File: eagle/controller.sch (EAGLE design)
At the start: 4 parts, among them IC1 MAX7219CNG

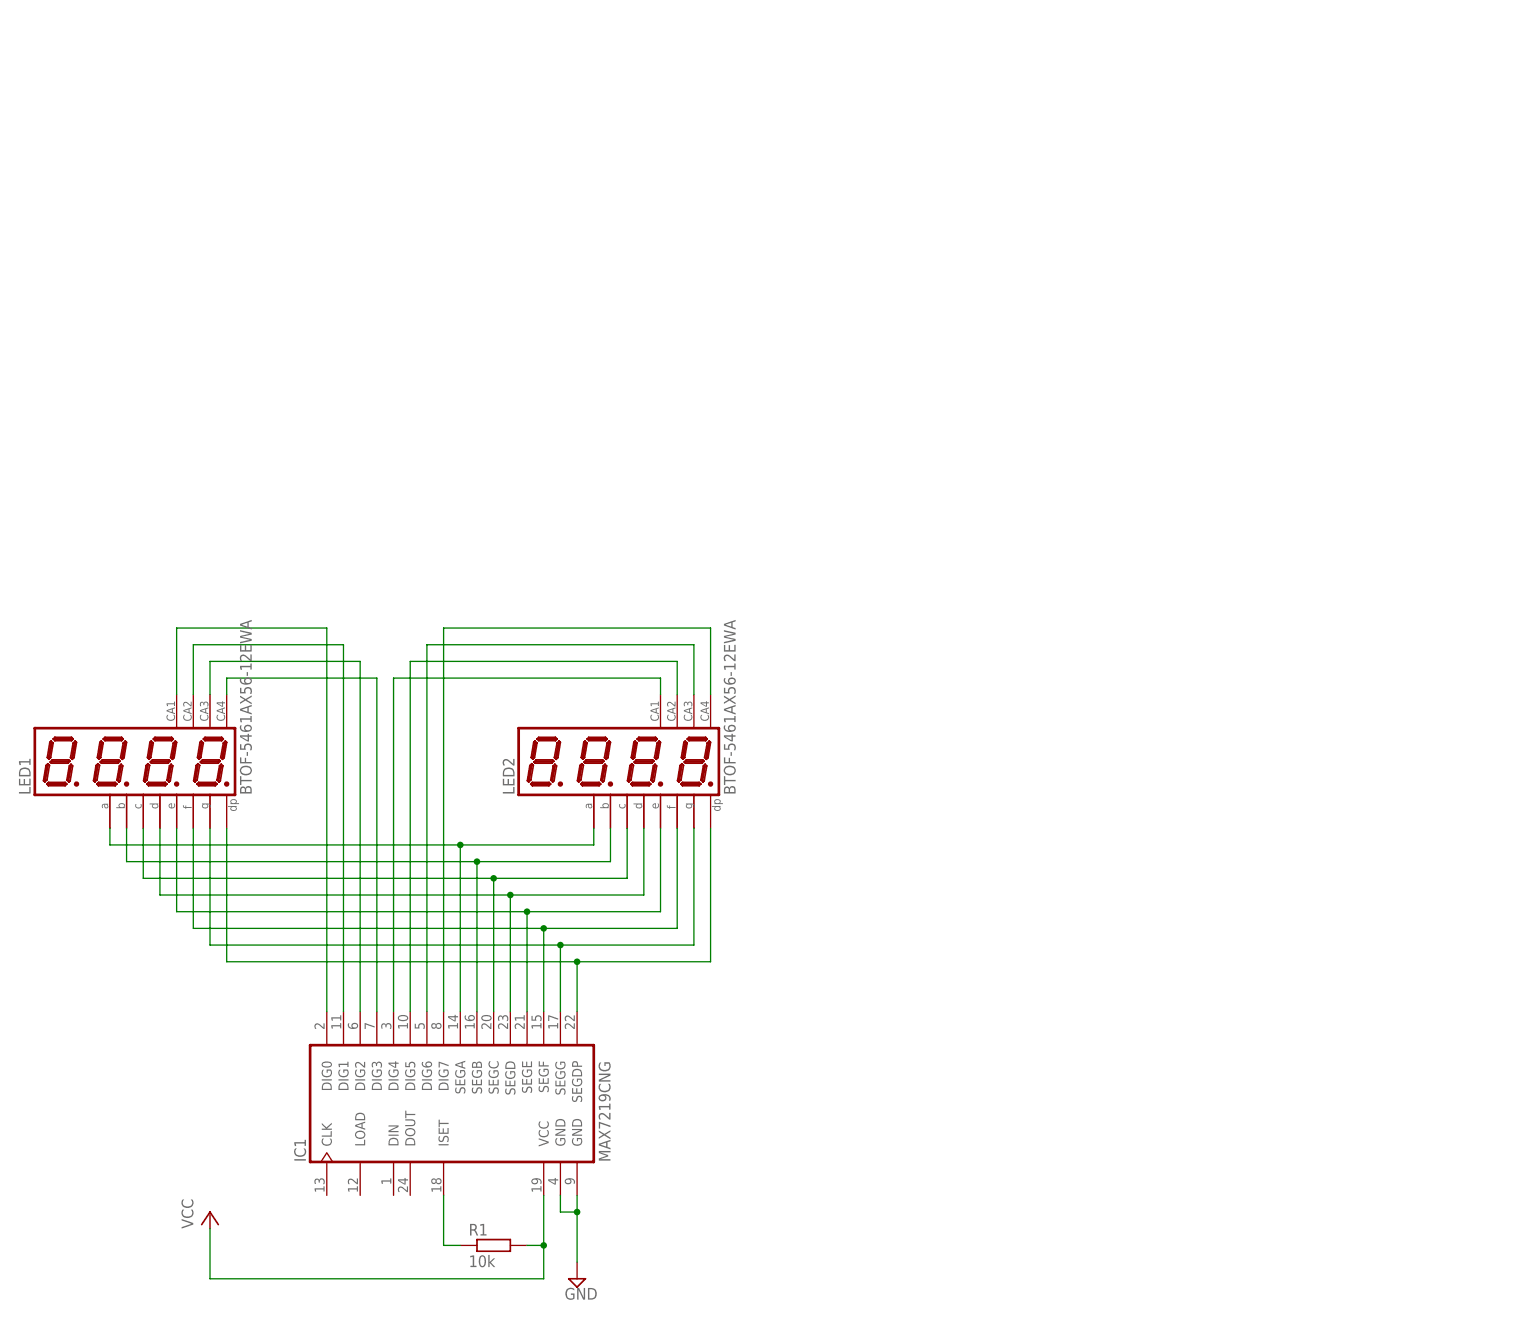
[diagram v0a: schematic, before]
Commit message: Add microcontroller to controller board schematic (still wip)
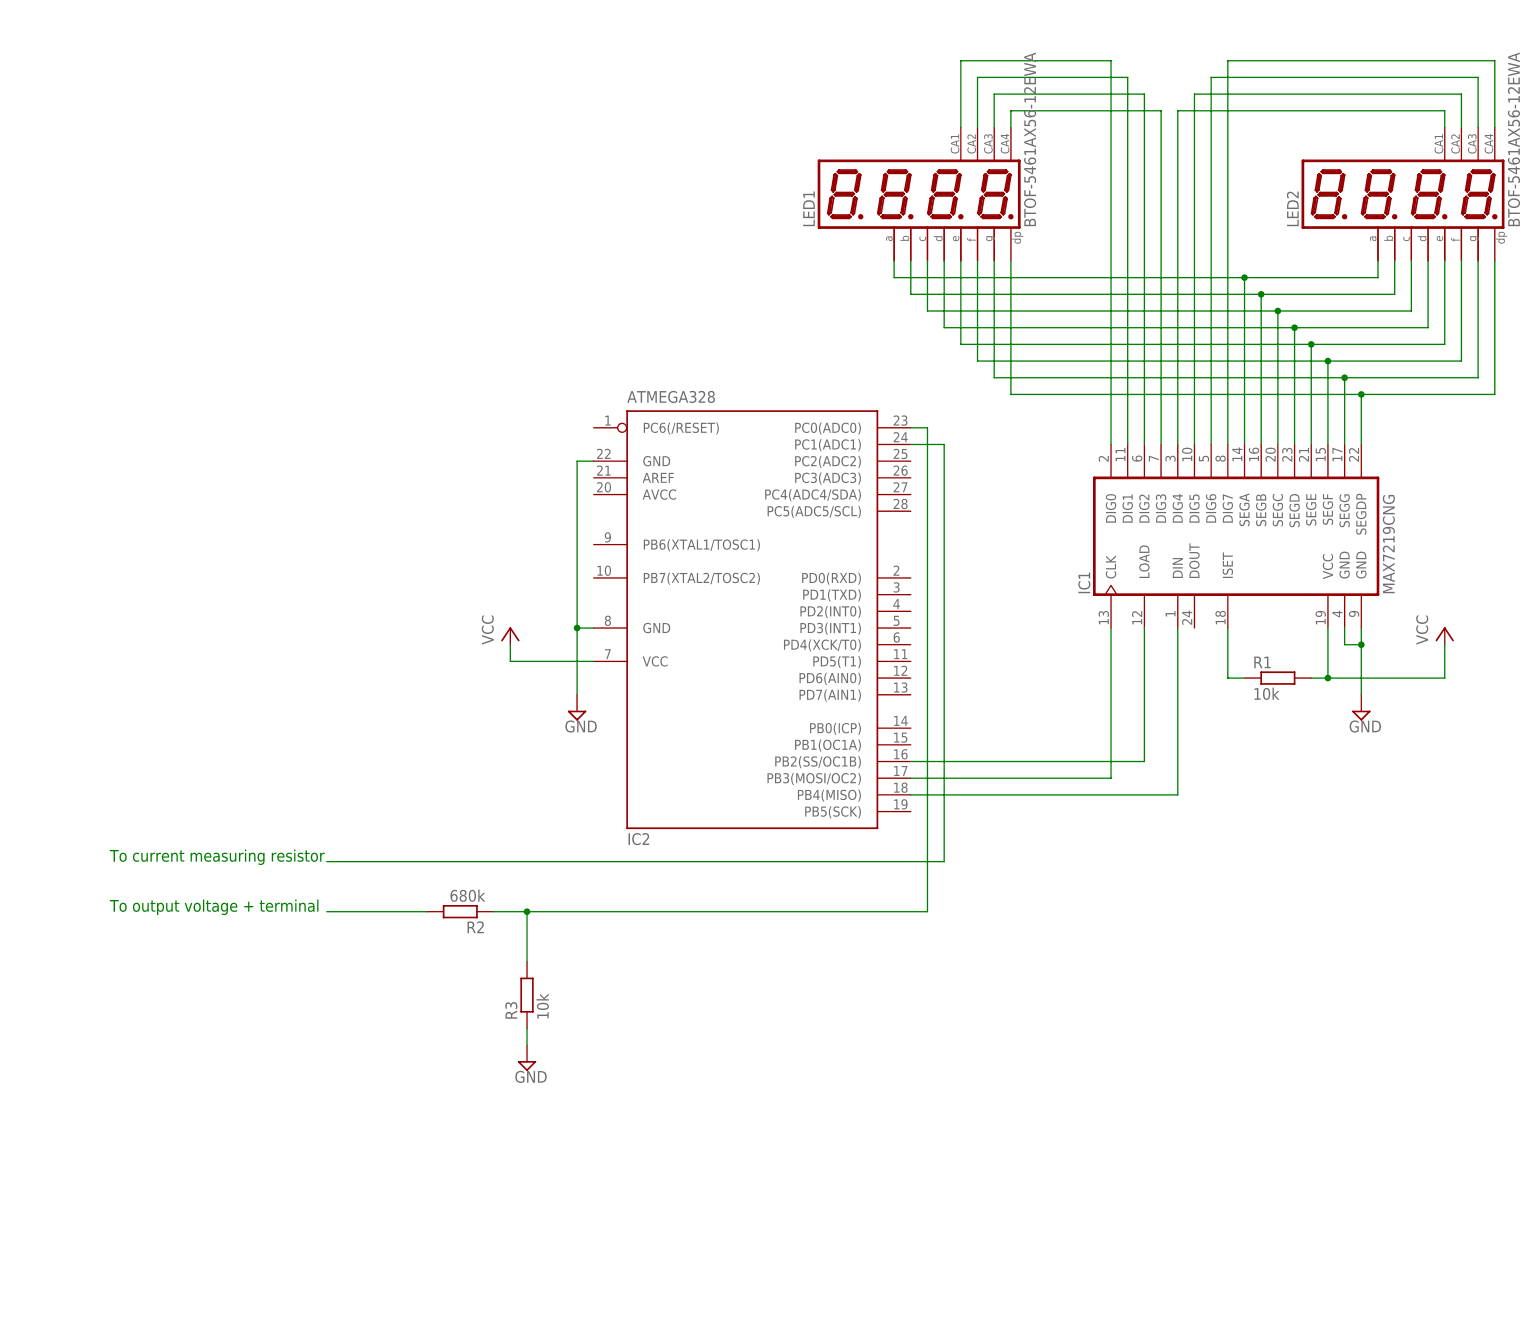
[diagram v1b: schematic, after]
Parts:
- added IC2: ATMEGA328, atmel:MEGA8-P
- added R2: 680k, rcl:R-EU_0207/10
- added R3: 10k, rcl:R-EU_0207/10
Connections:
- new net N$18: IC1.DIN, IC2.PB4(MISO)
- new net N$19: IC1.CLK, IC2.PB3(MOSI/OC2)
- new net N$20: IC1.LOAD, IC2.PB2(SS/OC1B)
- new net N$21: IC2.PC1(ADC1)
- new net N$22: IC2.PC0(ADC0), R2.1, R3.2
- new net N$23: R2.2
- net GND: now also IC2.GND, IC2.GND@1, R3.1
- net VCC: now also IC2.VCC@1
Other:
- note added: "To current measuring resistor"
- note added: "To output voltage + terminal"
- moved on the sheet: IC1, LED1, LED2, R1

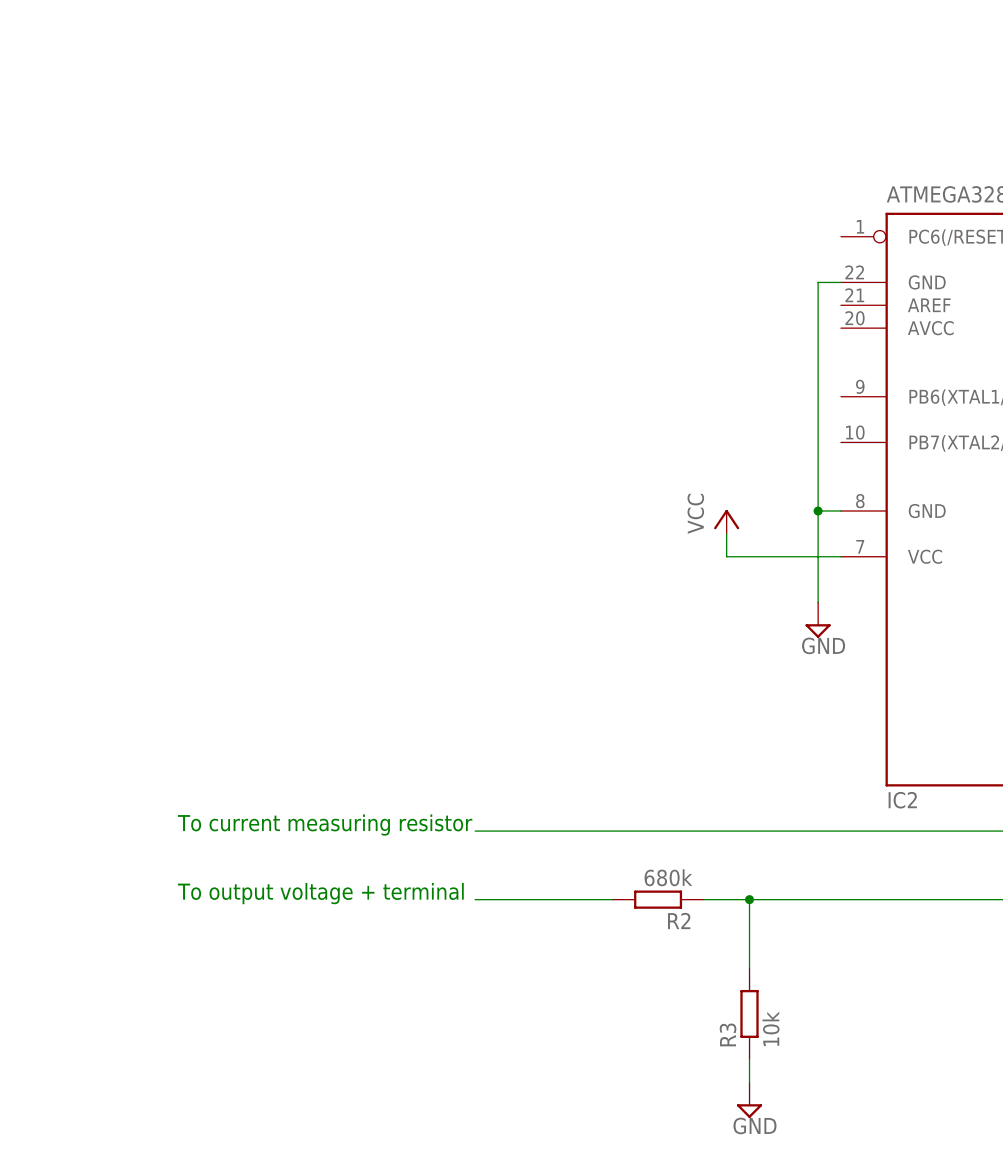
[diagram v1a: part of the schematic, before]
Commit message: More uC wiring + connector for controller schematic
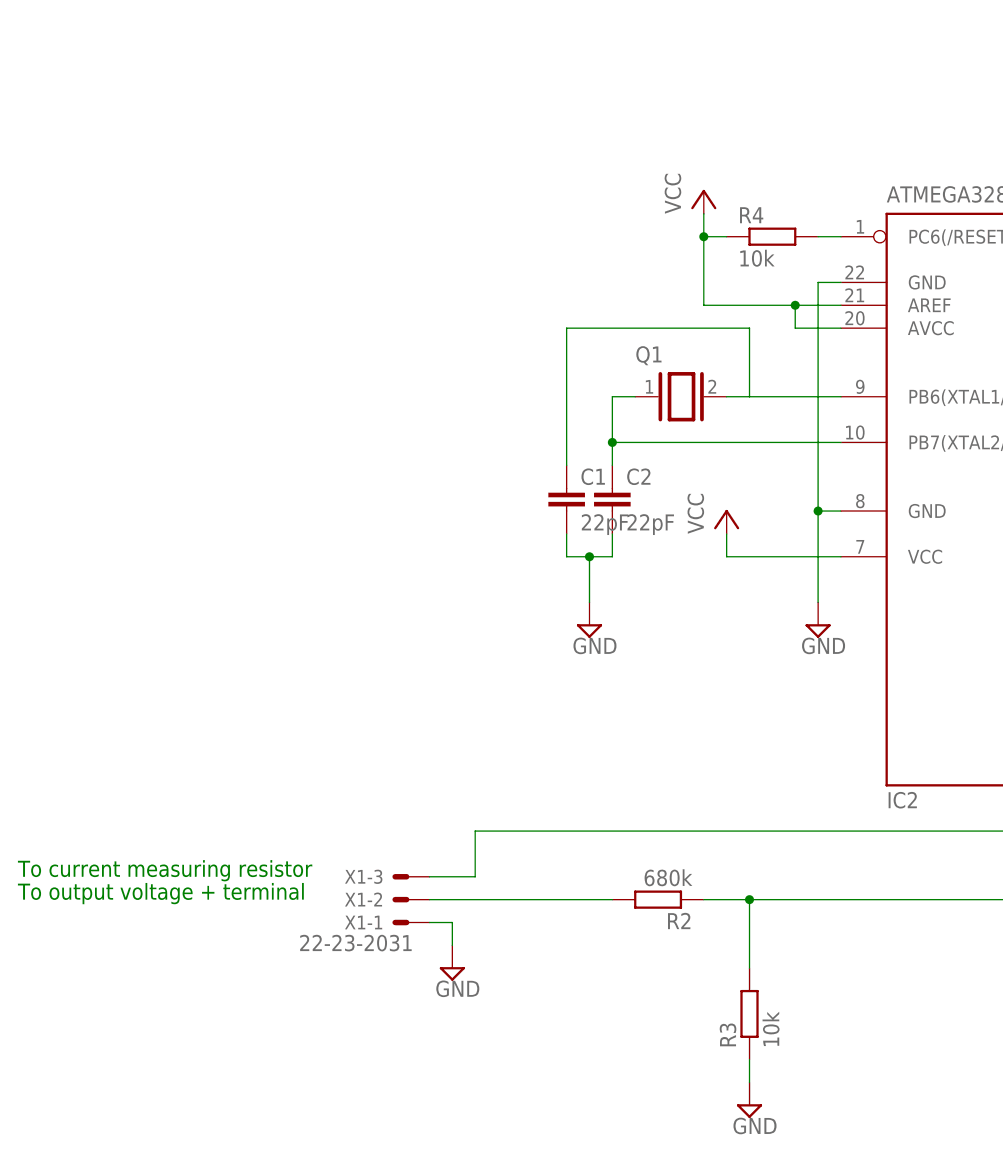
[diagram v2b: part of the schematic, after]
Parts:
- added C1, C2: 22pF, capacitor-wima:C2.5/2
- added Q1: (no value), special:XTAL/S
- added R4: 10k, rcl:R-EU_0207/10
- added X1: 22-23-2031, con-molex:22-23-2031
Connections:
- new net N$24: C1.1, IC2.PB6(XTAL1/TOSC1), Q1.2
- new net N$25: C2.1, IC2.PB7(XTAL2/TOSC2), Q1.1
- new net N$28: IC2.PC6(/RESET), R4.2
- net GND: now also C1.2, C2.2, X1-1.S
- net N$21: now also X1-3.S
- net N$23: now also X1-2.S
- net VCC: now also IC2.AREF, IC2.AVCC, R4.1
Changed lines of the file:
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@@
 <part name="R3" library="rcl" deviceset="R-EU_" device="0207/10" value="10k"/>
 <part name="SUPPLY3" library="supply2" deviceset="GND" device=""/>
+<part name="Q1" library="special" deviceset="XTAL/S" device=""/>
+<part name="C1" library="capacitor-wima" deviceset="C" device="2.5/2" value="22pF"/>
+<part name="C2" library="capacitor-wima" deviceset="C" device="2.5/2" value="22pF"/>
+<part name="SUPPLY4" library="supply2" deviceset="GND" device=""/>
+<part name="R4" library="rcl" deviceset="R-EU_" device="0207/10" value="10k"/>
+<part name="P+3" library="supply1" deviceset="VCC" device=""/>
+<part name="X1" library="con-molex" deviceset="22-23-2031" device=""/>
+<part name="SUPPLY5" library="supply2" deviceset="GND" device=""/>
 </parts>
 <sheets>
 <sheet>
 <plain>
-<text x="10.16" y="33.02" size="1.778" layer="91">To output voltage + terminal</text>
-<text x="10.16" y="40.64" size="1.778" layer="91">To current measuring resistor</text>
+<text x="-7.62" y="33.02" size="1.778" layer="91">To output voltage + terminal</text>
+<text x="-7.62" y="35.56" size="1.778" layer="91">To current measuring resistor</text>
 </plain>
 <instances>
@@
 <instance part="R3" gate="G$1" x="73.66" y="20.32" rot="R90"/>
 <instance part="SUPPLY3" gate="GND" x="73.66" y="10.16"/>
+<instance part="Q1" gate="G$1" x="66.04" y="88.9"/>
+<instance part="C1" gate="G$1" x="53.34" y="78.74"/>
+<instance part="C2" gate="G$1" x="58.42" y="78.74"/>
+<instance part="SUPPLY4" gate="GND" x="55.88" y="63.5"/>
+<instance part="R4" gate="G$1" x="76.2" y="106.68"/>
+<instance part="P+3" gate="VCC" x="68.58" y="111.76"/>
+<instance part="X1" gate="-1" x="35.56" y="30.48" rot="R180"/>
+<instance part="X1" gate="-2" x="35.56" y="33.02" rot="R180"/>
+<instance part="X1" gate="-3" x="35.56" y="35.56" rot="R180"/>
+<instance part="SUPPLY5" gate="GND" x="40.64" y="25.4"/>
 </instances>
 <busses>
@@
 <wire x1="73.66" y1="15.24" x2="73.66" y2="12.7" width="0.1524" layer="91"/>
 </segment>
+<segment>
+<pinref part="C1" gate="G$1" pin="2"/>
+<wire x1="53.34" y1="73.66" x2="53.34" y2="71.12" width="0.1524" layer="91"/>
+<wire x1="53.34" y1="71.12" x2="55.88" y2="71.12" width="0.1524" layer="91"/>
+<pinref part="C2" gate="G$1" pin="2"/>
+<wire x1="55.88" y1="71.12" x2="58.42" y2="71.12" width="0.1524" layer="91"/>
+<wire x1="58.42" y1="71.12" x2="58.42" y2="73.66" width="0.1524" layer="91"/>
+<wire x1="55.88" y1="71.12" x2="55.88" y2="66.04" width="0.1524" layer="91"/>
+<junction x="55.88" y="71.12"/>
+<pinref part="SUPPLY4" gate="GND" pin="GND"/>
+</segment>
+<segment>
+<pinref part="X1" gate="-1" pin="S"/>
+<pinref part="SUPPLY5" gate="GND" pin="GND"/>
+<wire x1="38.1" y1="30.48" x2="40.64" y2="30.48" width="0.1524" layer="91"/>
+<wire x1="40.64" y1="30.48" x2="40.64" y2="27.94" width="0.1524" layer="91"/>
+</segment>
 </net>
 <net name="VCC" class="0">
@@
 <wire x1="83.82" y1="71.12" x2="71.12" y2="71.12" width="0.1524" layer="91"/>
 <wire x1="71.12" y1="71.12" x2="71.12" y2="73.66" width="0.1524" layer="91"/>
+</segment>
+<segment>
+<pinref part="P+3" gate="VCC" pin="VCC"/>
+<wire x1="68.58" y1="109.22" x2="68.58" y2="106.68" width="0.1524" layer="91"/>
+<pinref part="R4" gate="G$1" pin="1"/>
+<wire x1="68.58" y1="106.68" x2="71.12" y2="106.68" width="0.1524" layer="91"/>
+<pinref part="IC2" gate="G$1" pin="AVCC"/>
+<wire x1="83.82" y1="96.52" x2="78.74" y2="96.52" width="0.1524" layer="91"/>
+<wire x1="78.74" y1="96.52" x2="78.74" y2="99.06" width="0.1524" layer="91"/>
+<pinref part="IC2" gate="G$1" pin="AREF"/>
+<wire x1="78.74" y1="99.06" x2="83.82" y2="99.06" width="0.1524" layer="91"/>
+<wire x1="78.74" y1="99.06" x2="68.58" y2="99.06" width="0.1524" layer="91"/>
+<wire x1="68.58" y1="99.06" x2="68.58" y2="106.68" width="0.1524" layer="91"/>
+<junction x="78.74" y="99.06"/>
+<junction x="68.58" y="106.68"/>
 </segment>
 </net>
@@
 <segment>
 <pinref part="R2" gate="G$1" pin="2"/>
-<wire x1="58.42" y1="33.02" x2="43.18" y2="33.02" width="0.1524" layer="91"/>
+<wire x1="58.42" y1="33.02" x2="38.1" y2="33.02" width="0.1524" layer="91"/>
+<pinref part="X1" gate="-2" pin="S"/>
 </segment>
 </net>
@@
 <wire x1="137.16" y1="104.14" x2="137.16" y2="40.64" width="0.1524" layer="91"/>
 <wire x1="137.16" y1="40.64" x2="43.18" y2="40.64" width="0.1524" layer="91"/>
-</segment>
-</net>
+<pinref part="X1" gate="-3" pin="S"/>
+<wire x1="38.1" y1="35.56" x2="43.18" y2="35.56" width="0.1524" layer="91"/>
+<wire x1="43.18" y1="35.56" x2="43.18" y2="40.64" width="0.1524" layer="91"/>
+</segment>
+</net>
+<net name="N$24" class="0">
+<segment>
+<pinref part="IC2" gate="G$1" pin="PB6(XTAL1/TOSC1)"/>
+<pinref part="Q1" gate="G$1" pin="2"/>
+<wire x1="83.82" y1="88.9" x2="73.66" y2="88.9" width="0.1524" layer="91"/>
+<pinref part="C1" gate="G$1" pin="1"/>
+<wire x1="73.66" y1="88.9" x2="71.12" y2="88.9" width="0.1524" layer="91"/>
+<wire x1="53.34" y1="81.28" x2="53.34" y2="96.52" width="0.1524" layer="91"/>
+<wire x1="53.34" y1="96.52" x2="73.66" y2="96.52" width="0.1524" layer="91"/>
+<wire x1="73.66" y1="96.52" x2="73.66" y2="88.9" width="0.1524" layer="91"/>
+</segment>
+</net>
+<net name="N$25" class="0">
+<segment>
+<pinref part="IC2" gate="G$1" pin="PB7(XTAL2/TOSC2)"/>
+<wire x1="83.82" y1="83.82" x2="58.42" y2="83.82" width="0.1524" layer="91"/>
+<wire x1="58.42" y1="83.82" x2="58.42" y2="88.9" width="0.1524" layer="91"/>
+<pinref part="Q1" gate="G$1" pin="1"/>
+<wire x1="58.42" y1="88.9" x2="60.96" y2="88.9" width="0.1524" layer="91"/>
+<pinref part="C2" gate="G$1" pin="1"/>
+<wire x1="58.42" y1="81.28" x2="58.42" y2="83.82" width="0.1524" layer="91"/>
+<junction x="58.42" y="83.82"/>
+</segment>
+</net>
+<net name="N$28" class="0">
+<segment>
+<pinref part="R4" gate="G$1" pin="2"/>
+<pinref part="IC2" gate="G$1" pin="PC6(/RESET)"/>
+<wire x1="81.28" y1="106.68" x2="83.82" y2="106.68" width="0.1524" layer="91"/>
+</segment>
+</net>
